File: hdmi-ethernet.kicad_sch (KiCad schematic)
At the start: 0 parts

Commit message: Add ETH PHY
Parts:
- added C? (x16): C_100n_0201, antmicro-footprints:0201-res, symbol antmicroCapacitorsmisc:C_100n_0201
- added C?: C_10n_0402, antmicro-footprints:0402-cap, symbol antmicroCapacitors0402:C_10n_0402
- added C? (x5): C_10u_0402, antmicro-footprints:0402-cap, symbol antmicroCapacitors0402:C_10u_0402
- added C? (x2): C_22p_0402, antmicro-footprints:0402-cap, symbol antmicroCapacitors0402:C_22p_0402
- added FB? (x2): BLM18PG121SN1D, antmicro-footprints:0603-res, symbol antmicroFerriteBeadsandChips:BLM18PG121SN1D
- added J?: 5-2337992-8, antmicro-footprints:5-2337992-8, symbol antmicroModularConnectorsJacksWithMagnetics:5-2337992-8
- added R? (x2): R_220R_0603, antmicro-footprints:0603-res, symbol antmicroResistors0603:R_220R_0603
- added R?: R_12k_0402, antmicro-footprints:0402-res, symbol antmicroResistors0402:R_12k_0402
- added R?: R_1M0_0402, antmicro-footprints:0402-res, symbol antmicroResistors0402:R_1M0_0402
- added U?: KSZ9131RNXC, antmicro-footprints:QFN-48-Microchip-QFN77-48LD-PL-2, symbol antmicroInterfaceControllers:KSZ9131RNXC
- added Y?: ABM8G-25.000MHZ-18-D2Y-T, antmicro-footprints:KX-7, symbol antmicroCrystals:ABM8G-25.000MHZ-18-D2Y-T
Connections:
- new net: R?.2, U?.48 (ISET)
- new net +3V3: R?.2, R?.2
- new net AVDDH: C?.1, C?.1, C?.1, C?.1, FB?.2, U?.1 (AVDDH), U?.12 (AVDDH), U?.47 (NC_(AVDDH))
- new net AVDDL: C?.1, C?.1, C?.1, C?.1, C?.1, C?.1, FB?.2, U?.4 (AVDDL), U?.44 (AVDDL_PLL), U?.9 (AVDDL)
- new net DVDDH: C?.1, C?.1, C?.1, C?.1, FB?.1, U?.16 (DVDDH), U?.34 (DVDDH), U?.40 (DVDDH)
- new net DVDDL: C?.1, C?.1, C?.1, C?.1, C?.1, C?.1, C?.1, FB?.1, U?.14 (NC_(DVDDL)), U?.18 (DVDDL), U?.23 (DVDDL), U?.26 (DVDDL), U?.30 (DVDDL), U?.39 (DVDDL)
- new net ETH1_N: J?.2 (P2), U?.3 (TXRXM_A)
- new net ETH1_P: J?.1 (P1), U?.2 (TXRXP_A)
- new net ETH2_N: J?.6 (P6), U?.6 (TXRXM_B)
- new net ETH2_P: J?.3 (P3), U?.5 (TXRXP_B)
- new net ETH3_N: J?.8 (P8), U?.8 (TXRXM_C)
- new net ETH3_P: J?.7 (P7), U?.7 (TXRXP_C)
- new net ETH4_N: J?.10 (P10), U?.11 (TXRXM_D)
- new net ETH4_P: J?.9 (P9), U?.10 (TXRXP_D)
- new net ETH_CONN_COMM: C?.1, J?.4 (P4), J?.5 (P5)
- new net ETH_RGMII.CLK125: U?.41 (CLK125_NDO/LED_MODE)
- new net ETH_RGMII.GTR_CLK: U?.35 (RX_CLK/PHYAD2)
- new net ETH_RGMII.GTX_CLK: U?.24 (GTX_CLK)
- new net ETH_RGMII.MDC: U?.36 (MDC)
- new net ETH_RGMII.MDIO: U?.37 (MDIO)
- new net ETH_RGMII.RXD0: U?.32 (RXD0/MODE0)
- new net ETH_RGMII.RXD1: U?.31 (RXD1/MODE1)
- new net ETH_RGMII.RXD2: U?.28 (RXD2/MODE2)
- new net ETH_RGMII.RXD3: U?.27 (RXD3/MODE3)
- new net ETH_RGMII.RX_DV: U?.33 (RX_DV/CLK125_EN)
- new net ETH_RGMII.TXD0: U?.19 (TXD0)
- new net ETH_RGMII.TXD1: U?.20 (TXD1)
- new net ETH_RGMII.TXD2: U?.21 (TXD2)
- new net ETH_RGMII.TXD3: U?.22 (TXD3)
- new net ETH_RGMII.TX_EN: U?.25 (TX_EN)
- new net ETH_RGMII.~{INT}: U?.38 (INT_N/PME_N2)
- new net ETH_RGMII.~{RESET}: U?.42 (RESET_N)
- new net ETH_XI: C?.1, R?.2, U?.46 (XI), Y?.1
- new net ETH_XO: C?.1, R?.1, U?.45 (XO), Y?.3
- new net GND: C?.2, C?.2, C?.2, C?.2, C?.2, C?.2, C?.2, C?.2, C?.2, C?.2, C?.2, C?.2, C?.2, C?.2, C?.2, C?.2, C?.2, C?.2, C?.2, C?.2, C?.2, C?.2, C?.2, C?.2, R?.1, U?.13 (NC_(GND)), U?.29 (GND), U?.49 (GND), Y?.2, Y?.4
- new net LED_LINK+: J?.17 (LED_YEL+), R?.1
- new net LED_LINK-: J?.18 (LED_YEL-), U?.17 (LED1/PHAD0/PME_N1)
- new net LED_SPD+: J?.15 (LED_GRN+), R?.1
- new net LED_SPD-: J?.16 (LED_GRN-), U?.15 (LED2/PHYAD1)
- new net POE.VC1: J?.11 (VC1)
- new net POE.VC2: J?.12 (VC2)
- new net POE.VC3: J?.13 (VC3)
- new net POE.VC4: J?.14 (VC4)
- no-connect marks 0 -> 1
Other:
- note added: "ETH PHY"
- note added: "NOTE: KSZ9131RNXC pins 13,14 and 47 connected for backward compability with KSZ9031RNXC"
- note added: "NOTE: Place close to AVDDL_PLL (PIN 44)"
- note added: "RJ45 connector with magnetics and PoE"
- note added: "TODO: - add power rails connections"

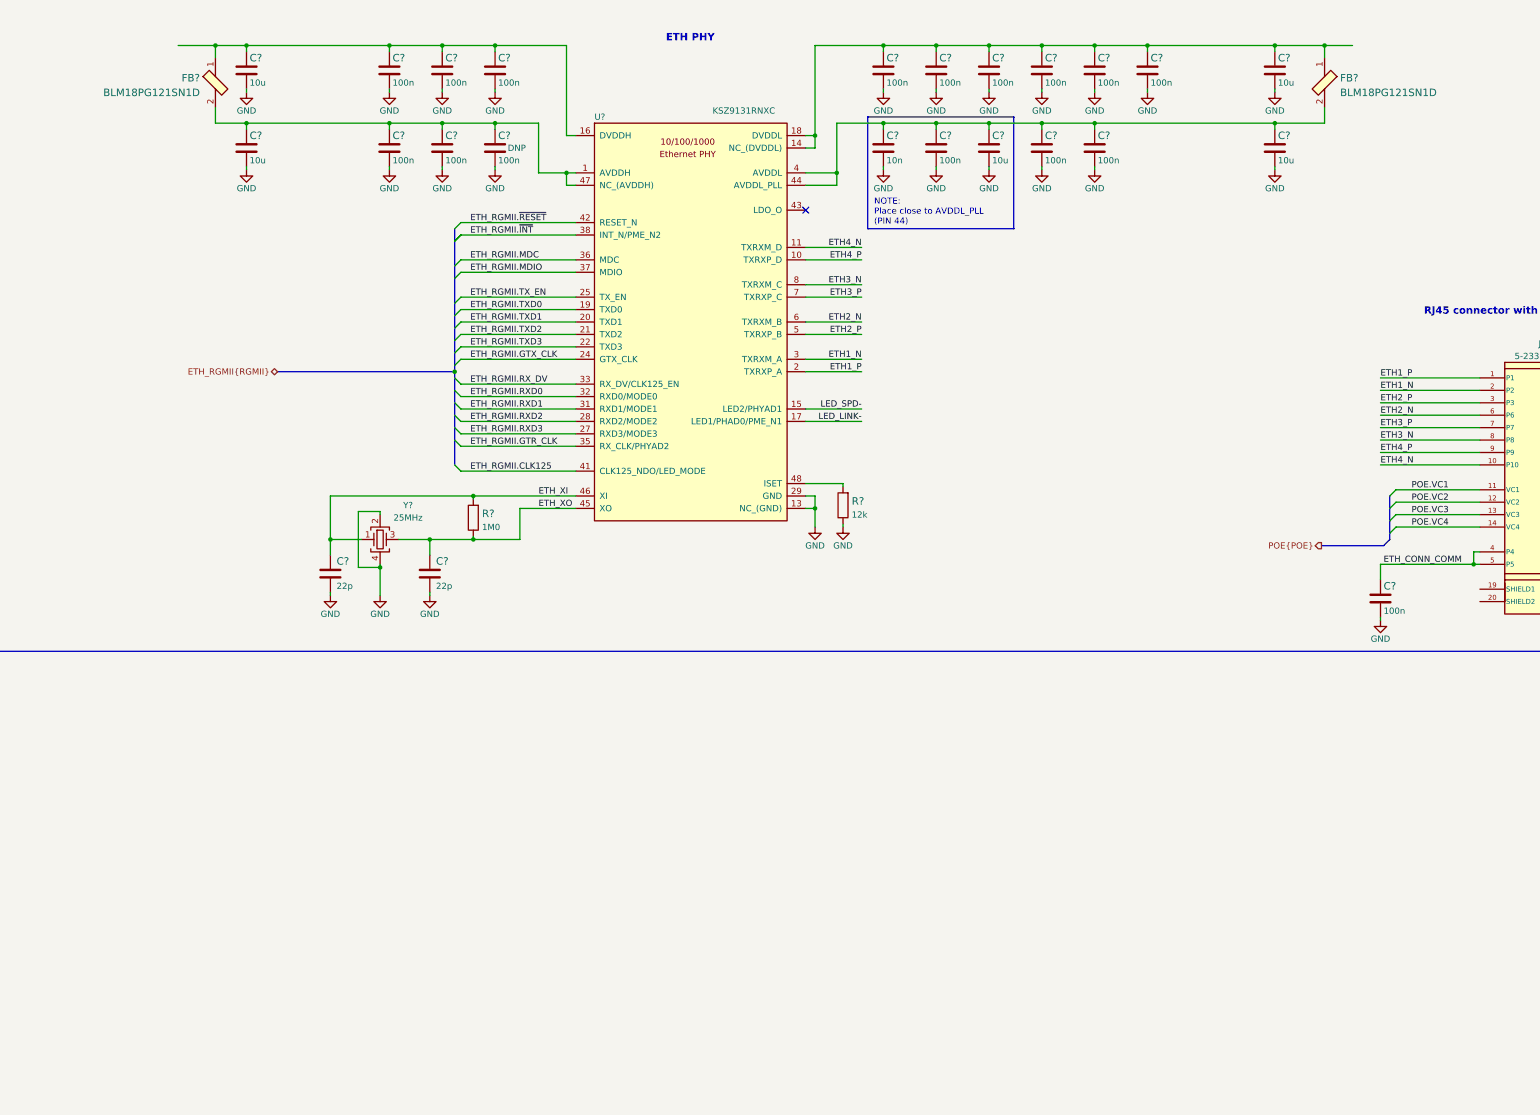
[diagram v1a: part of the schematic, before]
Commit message: Add HDMI connector
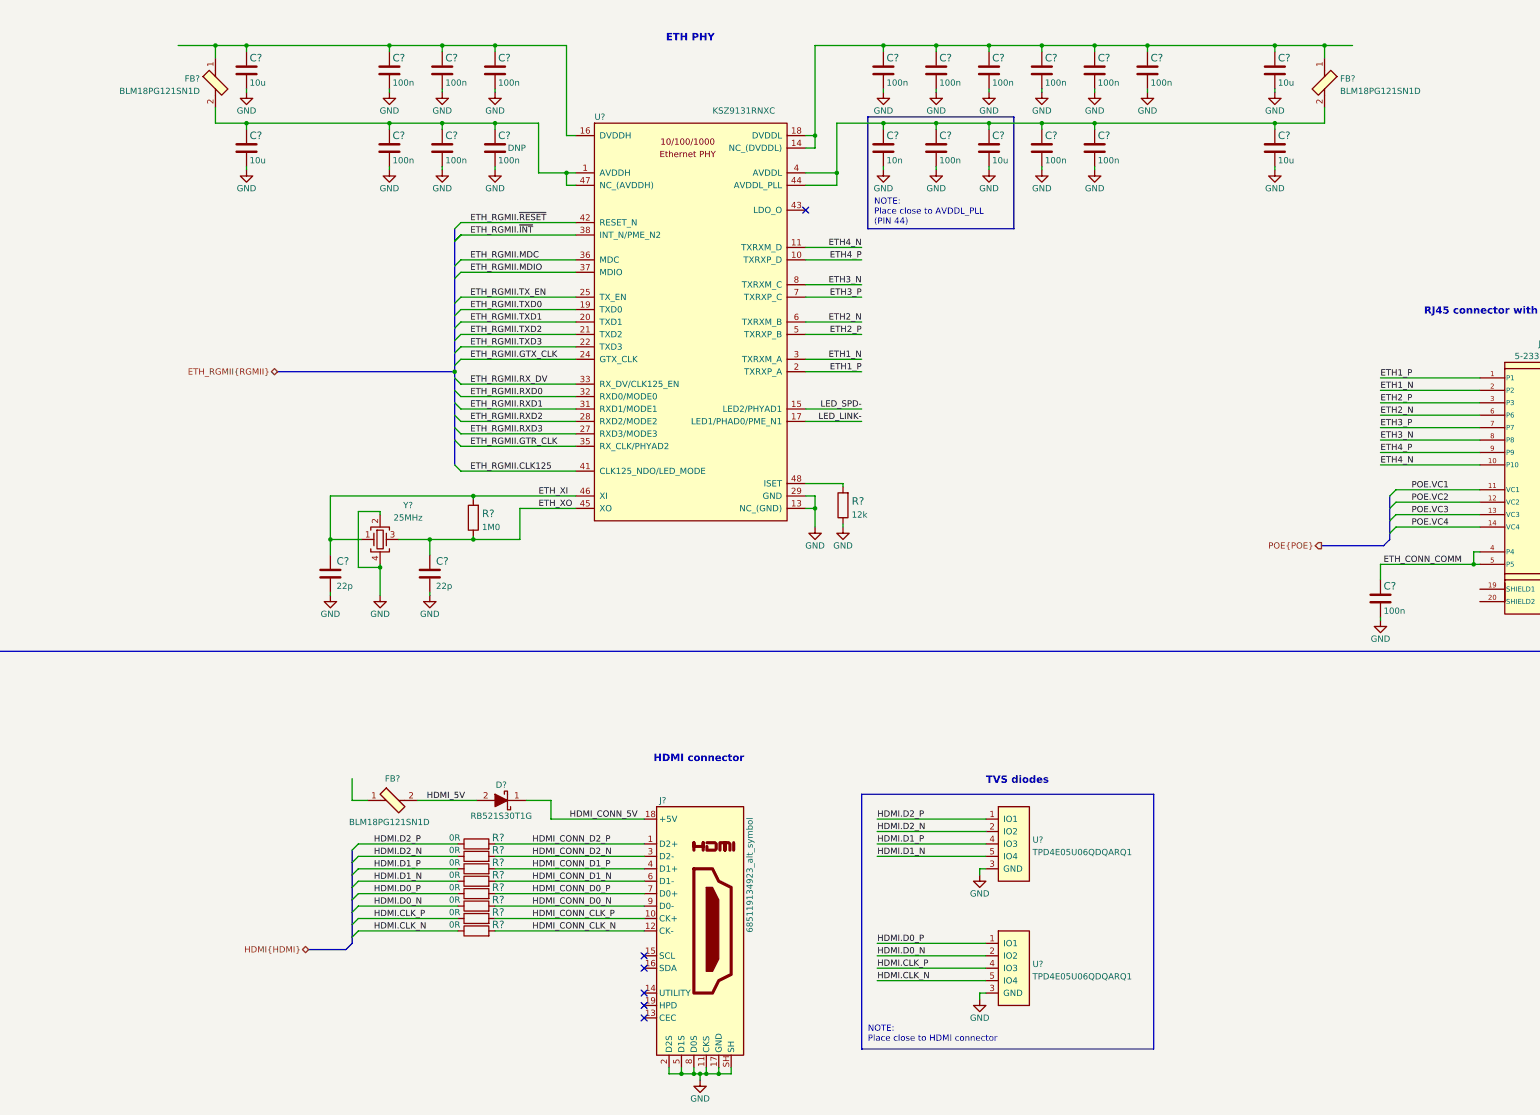
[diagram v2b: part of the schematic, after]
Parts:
- added D?: RB521S30T1G, antmicro-footprints:SOD-523, symbol antmicroDiodesRectifiersSingle:RB521S30T1G
- added FB?: BLM18PG121SN1D, antmicro-footprints:0603-res, symbol antmicroFerriteBeadsandChips:BLM18PG121SN1D
- added J?: 685119134923_alt_symbol, antmicro-footprints:HDMI_A_Female_685119134923, symbol antmicroUSBDVIHDMIConnectors:685119134923_alt_symbol
- added R? (x8): R_0R_0402, antmicro-footprints:0402-res, symbol antmicroResistors0402:R_0R_0402
- added U? (x2): TPD4E05U06QDQARQ1, antmicro-footprints:USON-10_2.5x1.0mm_P0.5mm, symbol antmicroTVSDiodes:TPD4E05U06QDQARQ1
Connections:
- net GND: now also J?.11 (CKS), J?.17 (GND), J?.2 (D2S), J?.5 (D1S), J?.8 (D0S), J?.SH, U?.3 (GND), U?.3 (GND), U?.8 (GND), U?.8 (GND)
- new net HDMI.CLK_N: R?.1, U?.5 (IO4), U?.6 (IO4)
- new net HDMI.CLK_P: R?.1, U?.4 (IO3), U?.7 (IO3)
- new net HDMI.D0_N: R?.1, U?.2 (IO2), U?.9 (IO2)
- new net HDMI.D0_P: R?.1, U?.1 (IO1), U?.10 (IO1)
- new net HDMI.D1_N: R?.1, U?.5 (IO4), U?.6 (IO4)
- new net HDMI.D1_P: R?.1, U?.4 (IO3), U?.7 (IO3)
- new net HDMI.D2_N: R?.1, U?.2 (IO2), U?.9 (IO2)
- new net HDMI.D2_P: R?.1, U?.1 (IO1), U?.10 (IO1)
- new net HDMI_5V: D?.2, FB?.2
- new net HDMI_CONN_5V: D?.1, J?.18 (+5V)
- new net HDMI_CONN_CLK_N: J?.12 (CK-), R?.2
- new net HDMI_CONN_CLK_P: J?.10 (CK+), R?.2
- new net HDMI_CONN_D0_N: J?.9 (D0-), R?.2
- new net HDMI_CONN_D0_P: J?.7 (D0+), R?.2
- new net HDMI_CONN_D1_N: J?.6 (D1-), R?.2
- new net HDMI_CONN_D1_P: J?.4 (D1+), R?.2
- new net HDMI_CONN_D2_N: J?.3 (D2-), R?.2
- new net HDMI_CONN_D2_P: J?.1 (D2+), R?.2
- no-connect marks 1 -> 6
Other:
- note added: "HDMI connector"
- note added: "NOTE: Place close to HDMI connector"
- note added: "TVS diodes"
